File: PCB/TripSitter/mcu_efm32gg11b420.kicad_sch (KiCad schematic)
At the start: 22 parts, among them J102 EFM32_PinHeader_PortE, J3 Conn_ARM_JTAG_SWD_20, SW1 SW_Push_Open, U3 IS62WVS2568FBLL-20NLI, U4 EFM32GG11B420F2048GQ100, Y101 48MHz

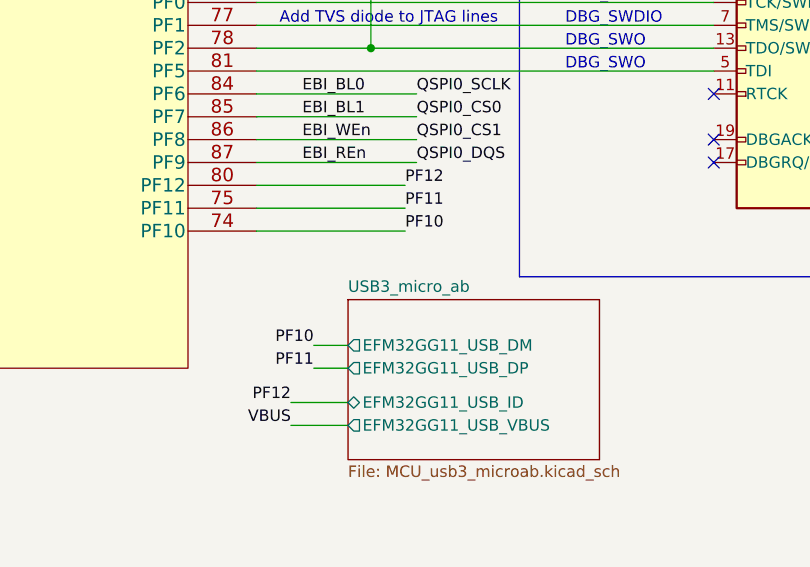
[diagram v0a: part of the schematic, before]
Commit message: change usb footprint to usb3 footprint
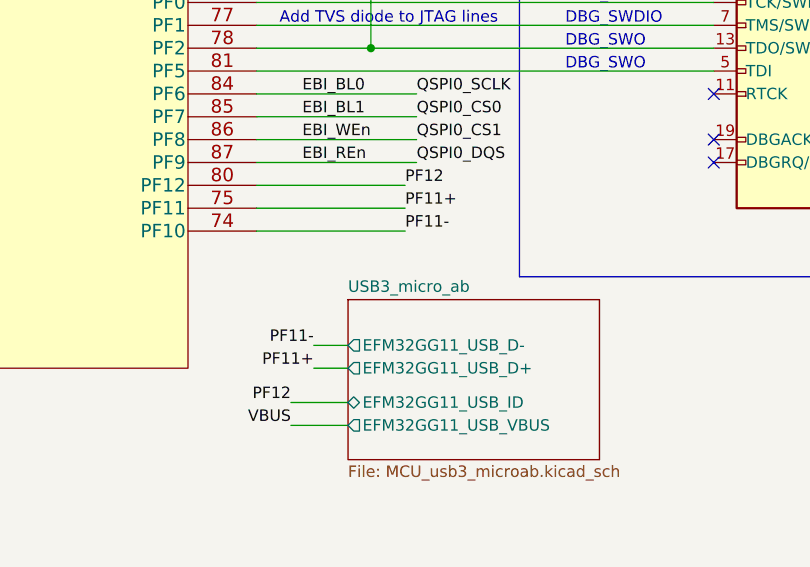
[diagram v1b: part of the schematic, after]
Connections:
- net PF10 renamed PF11-
- net PF11 renamed PF11+
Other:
- sheet USB3_micro_ab ports: added EFM32GG11_USB_D+, EFM32GG11_USB_D-; removed EFM32GG11_USB_DM, EFM32GG11_USB_DP
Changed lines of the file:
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@@
     (effects (font (size 1.27 1.27)) (justify right bottom))
   )
-  (label "PF11" (at 323.85 74.93 0) (fields_autoplaced)
+  (label "PF11+" (at 323.85 74.93 0) (fields_autoplaced)
     (effects (font (size 1.27 1.27)) (justify left bottom))
   )
@@
     (effects (font (size 1.27 1.27)) (justify left bottom))
   )
-  (label "PF11" (at 313.69 92.71 180) (fields_autoplaced)
+  (label "PF11+" (at 313.69 92.71 180) (fields_autoplaced)
     (effects (font (size 1.27 1.27)) (justify right bottom))
   )
@@
     (effects (font (size 1.27 1.27)) (justify right bottom))
   )
-  (label "PF10" (at 313.69 90.17 180) (fields_autoplaced)
+  (label "PF11-" (at 313.69 90.17 180) (fields_autoplaced)
     (effects (font (size 1.27 1.27)) (justify right bottom))
   )
@@
     (effects (font (size 1.27 1.27)) (justify right bottom))
   )
-  (label "PF10" (at 323.85 77.47 0) (fields_autoplaced)
+  (label "PF11-" (at 323.85 77.47 0) (fields_autoplaced)
     (effects (font (size 1.27 1.27)) (justify left bottom))
   )
@@
       (effects (font (size 1.27 1.27)) (justify left top))
     )
-    (pin "EFM32GG11_USB_DM" output (at 317.5 90.17 180)
+    (pin "EFM32GG11_USB_D-" output (at 317.5 90.17 180)
       (effects (font (size 1.27 1.27)) (justify left))
     )
@@
       (effects (font (size 1.27 1.27)) (justify left))
     )
-    (pin "EFM32GG11_USB_DP" output (at 317.5 92.71 180)
-      (effects (font (size 1.27 1.27)) (justify left))
-    )
+    (pin "EFM32GG11_USB_D+" output (at 317.5 92.71 180)
+      (effects (font (size 1.27 1.27)) (justify left))
+    )
